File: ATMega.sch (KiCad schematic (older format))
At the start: 28 parts, among them J14 Conn_02x03_Odd_Even, SW1 SW_Push, U2 ATmega2560-16AU, Y1 16MHz

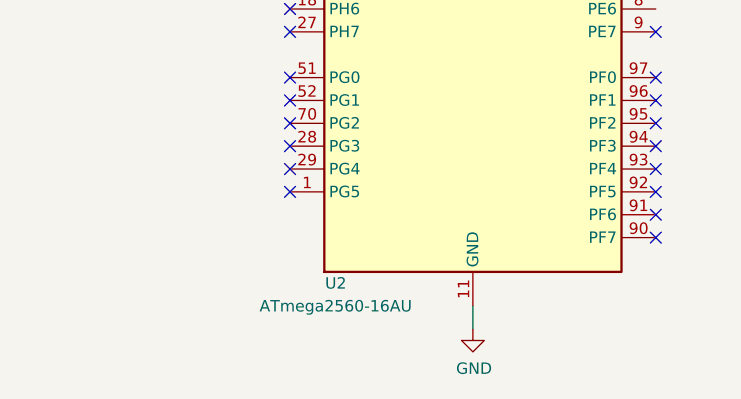
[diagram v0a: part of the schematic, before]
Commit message: LMZM23600 from official kicad lib
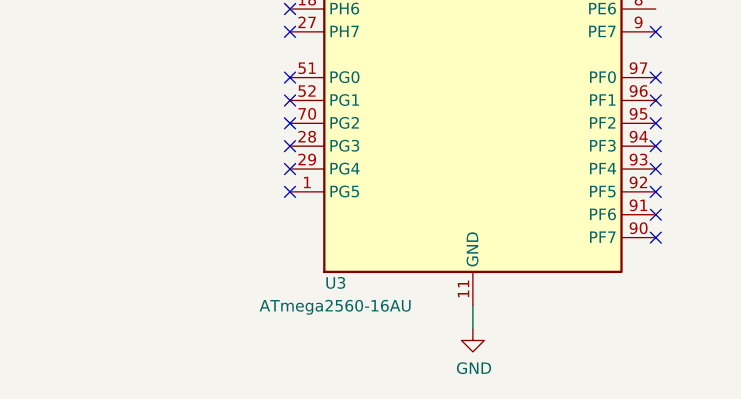
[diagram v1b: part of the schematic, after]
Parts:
- renumbered U2 to U3
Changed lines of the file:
@@
 	4300 5350 4250 5350
 $Comp
-L MCU_Microchip_ATmega:ATmega2560-16AU U2
+L MCU_Microchip_ATmega:ATmega2560-16AU U3
 U 1 1 5C280BF8
 P 3450 3950
-F 0 "U2" H 2850 1150 50  0000 C CNN
+F 0 "U3" H 2850 1150 50  0000 C CNN
 F 1 "ATmega2560-16AU" H 2850 1050 50  0000 C CNN
 F 2 "Package_QFP:TQFP-100_14x14mm_P0.5mm" H 3450 3950 50  0001 C CIN

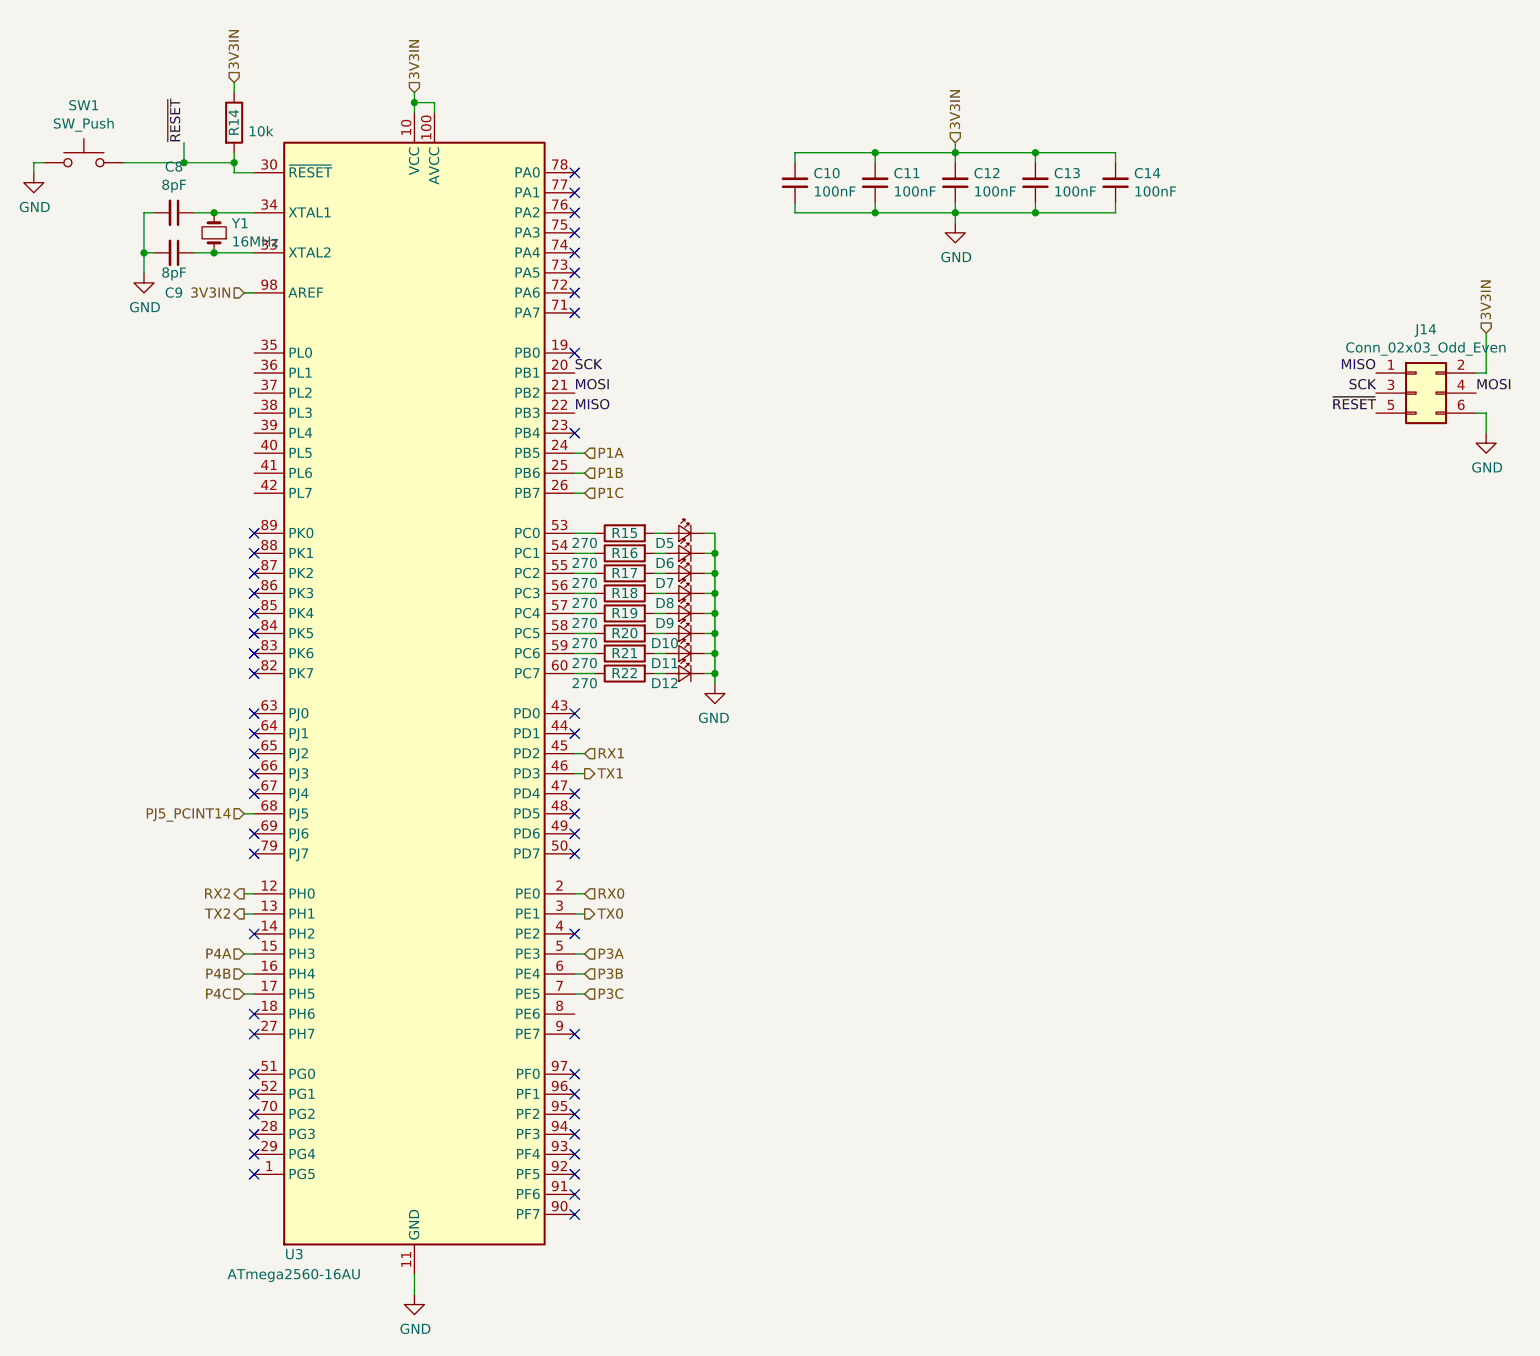
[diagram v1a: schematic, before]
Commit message: use submodule for FT230
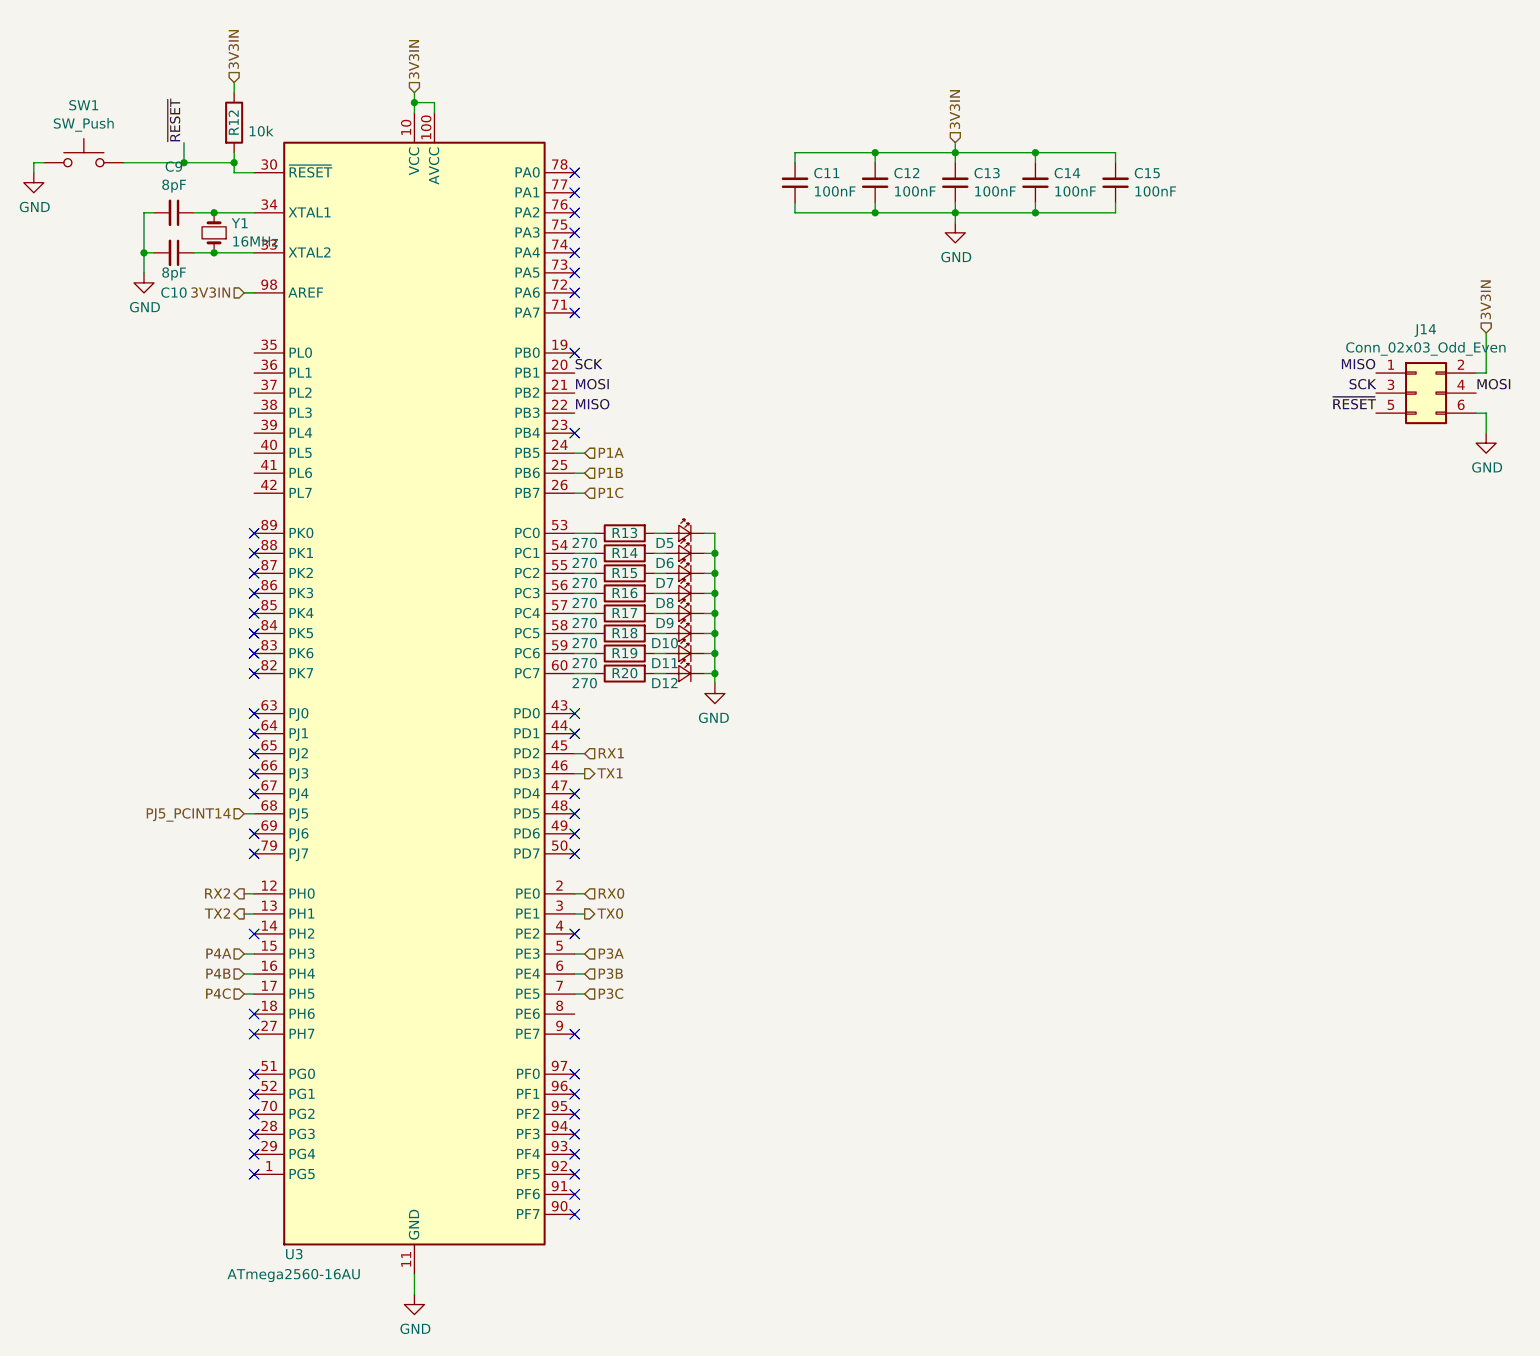
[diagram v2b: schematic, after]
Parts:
- renumbered C9 to C10, C10 to C11, C11 to C12, C12 to C13, C13 to C14, C14 to C15, C8 to C9, R14 to R12, R15 to R13, R16 to R14, R17 to R15, R18 to R16, R19 to R17, R20 to R18, R21 to R19, R22 to R20
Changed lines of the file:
@@
 	2450 1750 2650 1750
 $Comp
-L Device:C_Small C8
+L Device:C_Small C9
 U 1 1 5C2814DA
 P 2250 1550
-F 0 "C8" V 2021 1550 50  0000 C CNN
+F 0 "C9" V 2021 1550 50  0000 C CNN
 F 1 "8pF" V 2112 1550 50  0000 C CNN
 F 2 "Capacitor_SMD:C_0603_1608Metric" H 2250 1550 50  0001 C CNN
@@
 $EndComp
 $Comp
-L Device:C_Small C9
+L Device:C_Small C10
 U 1 1 5C281519
 P 2250 1750
-F 0 "C9" V 2450 1750 50  0000 C CNN
+F 0 "C10" V 2450 1750 50  0000 C CNN
 F 1 "8pF" V 2350 1750 50  0000 C CNN
 F 2 "Capacitor_SMD:C_0603_1608Metric" H 2250 1750 50  0001 C CNN
@@
 Connection ~ 2100 1750
 $Comp
-L Device:R R15
+L Device:R R13
 U 1 1 5C281CF1
 P 4500 3150
-F 0 "R15" V 4500 3150 50  0000 C CNN
+F 0 "R13" V 4500 3150 50  0000 C CNN
 F 1 "270" V 4550 3350 50  0000 C CNN
 F 2 "Resistor_SMD:R_0603_1608Metric" V 4430 3150 50  0001 C CNN
@@
 $EndComp
 $Comp
-L Device:R R16
+L Device:R R14
 U 1 1 5C281E2C
 P 4500 3250
-F 0 "R16" V 4500 3250 50  0000 C CNN
+F 0 "R14" V 4500 3250 50  0000 C CNN
 F 1 "270" V 4550 3450 50  0000 C CNN
 F 2 "Resistor_SMD:R_0603_1608Metric" V 4430 3250 50  0001 C CNN
@@
 $EndComp
 $Comp
-L Device:R R17
+L Device:R R15
 U 1 1 5C281E58
 P 4500 3350
-F 0 "R17" V 4500 3350 50  0000 C CNN
+F 0 "R15" V 4500 3350 50  0000 C CNN
 F 1 "270" V 4550 3550 50  0000 C CNN
 F 2 "Resistor_SMD:R_0603_1608Metric" V 4430 3350 50  0001 C CNN
@@
 $EndComp
 $Comp
-L Device:R R18
+L Device:R R16
 U 1 1 5C281E76
 P 4500 3450
-F 0 "R18" V 4500 3450 50  0000 C CNN
+F 0 "R16" V 4500 3450 50  0000 C CNN
 F 1 "270" V 4550 3650 50  0000 C CNN
 F 2 "Resistor_SMD:R_0603_1608Metric" V 4430 3450 50  0001 C CNN
@@
 	4950 3450 4950 3350
 $Comp
-L Device:R R14
+L Device:R R12
 U 1 1 5C28BE77
 P 2550 1100
-F 0 "R14" V 2550 1100 50  0000 C CNN
+F 0 "R12" V 2550 1100 50  0000 C CNN
 F 1 "10k" H 2620 1055 50  0000 L CNN
 F 2 "Resistor_SMD:R_0603_1608Metric" V 2480 1100 50  0001 C CNN
@@
 	2600 1950 2650 1950
 $Comp
-L Device:C_Small C10
+L Device:C_Small C11
 U 1 1 5C28F5ED
 P 5350 1400
-F 0 "C10" H 5258 1354 50  0000 R CNN
+F 0 "C11" H 5258 1354 50  0000 R CNN
 F 1 "100nF" H 5258 1445 50  0000 R CNN
 F 2 "Capacitor_SMD:C_0603_1608Metric" H 5350 1400 50  0001 C CNN
@@
 $EndComp
 $Comp
-L Device:C_Small C11
+L Device:C_Small C12
 U 1 1 5C28FBD2
 P 5750 1400
-F 0 "C11" H 5658 1354 50  0000 R CNN
+F 0 "C12" H 5658 1354 50  0000 R CNN
 F 1 "100nF" H 5658 1445 50  0000 R CNN
 F 2 "Capacitor_SMD:C_0603_1608Metric" H 5750 1400 50  0001 C CNN
@@
 $EndComp
 $Comp
-L Device:C_Small C12
+L Device:C_Small C13
 U 1 1 5C28FC1A
 P 6150 1400
-F 0 "C12" H 6058 1354 50  0000 R CNN
+F 0 "C13" H 6058 1354 50  0000 R CNN
 F 1 "100nF" H 6058 1445 50  0000 R CNN
 F 2 "Capacitor_SMD:C_0603_1608Metric" H 6150 1400 50  0001 C CNN
@@
 $EndComp
 $Comp
-L Device:C_Small C13
+L Device:C_Small C14
 U 1 1 5C28FC66
 P 6550 1400
-F 0 "C13" H 6458 1354 50  0000 R CNN
+F 0 "C14" H 6458 1354 50  0000 R CNN
 F 1 "100nF" H 6458 1445 50  0000 R CNN
 F 2 "Capacitor_SMD:C_0603_1608Metric" H 6550 1400 50  0001 C CNN
@@
 $EndComp
 $Comp
-L Device:C_Small C14
+L Device:C_Small C15
 U 1 1 5C28FCBA
 P 6950 1400
-F 0 "C14" H 6858 1354 50  0000 R CNN
+F 0 "C15" H 6858 1354 50  0000 R CNN
 F 1 "100nF" H 6858 1445 50  0000 R CNN
 F 2 "Capacitor_SMD:C_0603_1608Metric" H 6950 1400 50  0001 C CNN
@@
 NoConn ~ 4250 6550
 $Comp
-L Device:R R19
+L Device:R R17
 U 1 1 5C923641
 P 4500 3550
-F 0 "R19" V 4500 3550 50  0000 C CNN
+F 0 "R17" V 4500 3550 50  0000 C CNN
 F 1 "270" V 4550 3750 50  0000 C CNN
 F 2 "Resistor_SMD:R_0603_1608Metric" V 4430 3550 50  0001 C CNN
@@
 $EndComp
 $Comp
-L Device:R R20
+L Device:R R18
 U 1 1 5C923A5C
 P 4500 3650
-F 0 "R20" V 4500 3650 50  0000 C CNN
+F 0 "R18" V 4500 3650 50  0000 C CNN
 F 1 "270" V 4550 3850 50  0000 C CNN
 F 2 "Resistor_SMD:R_0603_1608Metric" V 4430 3650 50  0001 C CNN
@@
 $EndComp
 $Comp
-L Device:R R21
+L Device:R R19
 U 1 1 5C923B7C
 P 4500 3750
-F 0 "R21" V 4500 3750 50  0000 C CNN
+F 0 "R19" V 4500 3750 50  0000 C CNN
 F 1 "270" V 4550 3950 50  0000 C CNN
 F 2 "Resistor_SMD:R_0603_1608Metric" V 4430 3750 50  0001 C CNN
@@
 $EndComp
 $Comp
-L Device:R R22
+L Device:R R20
 U 1 1 5C923CFF
 P 4500 3850
-F 0 "R22" V 4500 3850 50  0000 C CNN
+F 0 "R20" V 4500 3850 50  0000 C CNN
 F 1 "270" V 4550 4050 50  0000 C CNN
 F 2 "Resistor_SMD:R_0603_1608Metric" V 4430 3850 50  0001 C CNN

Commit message: pullups, jumpers
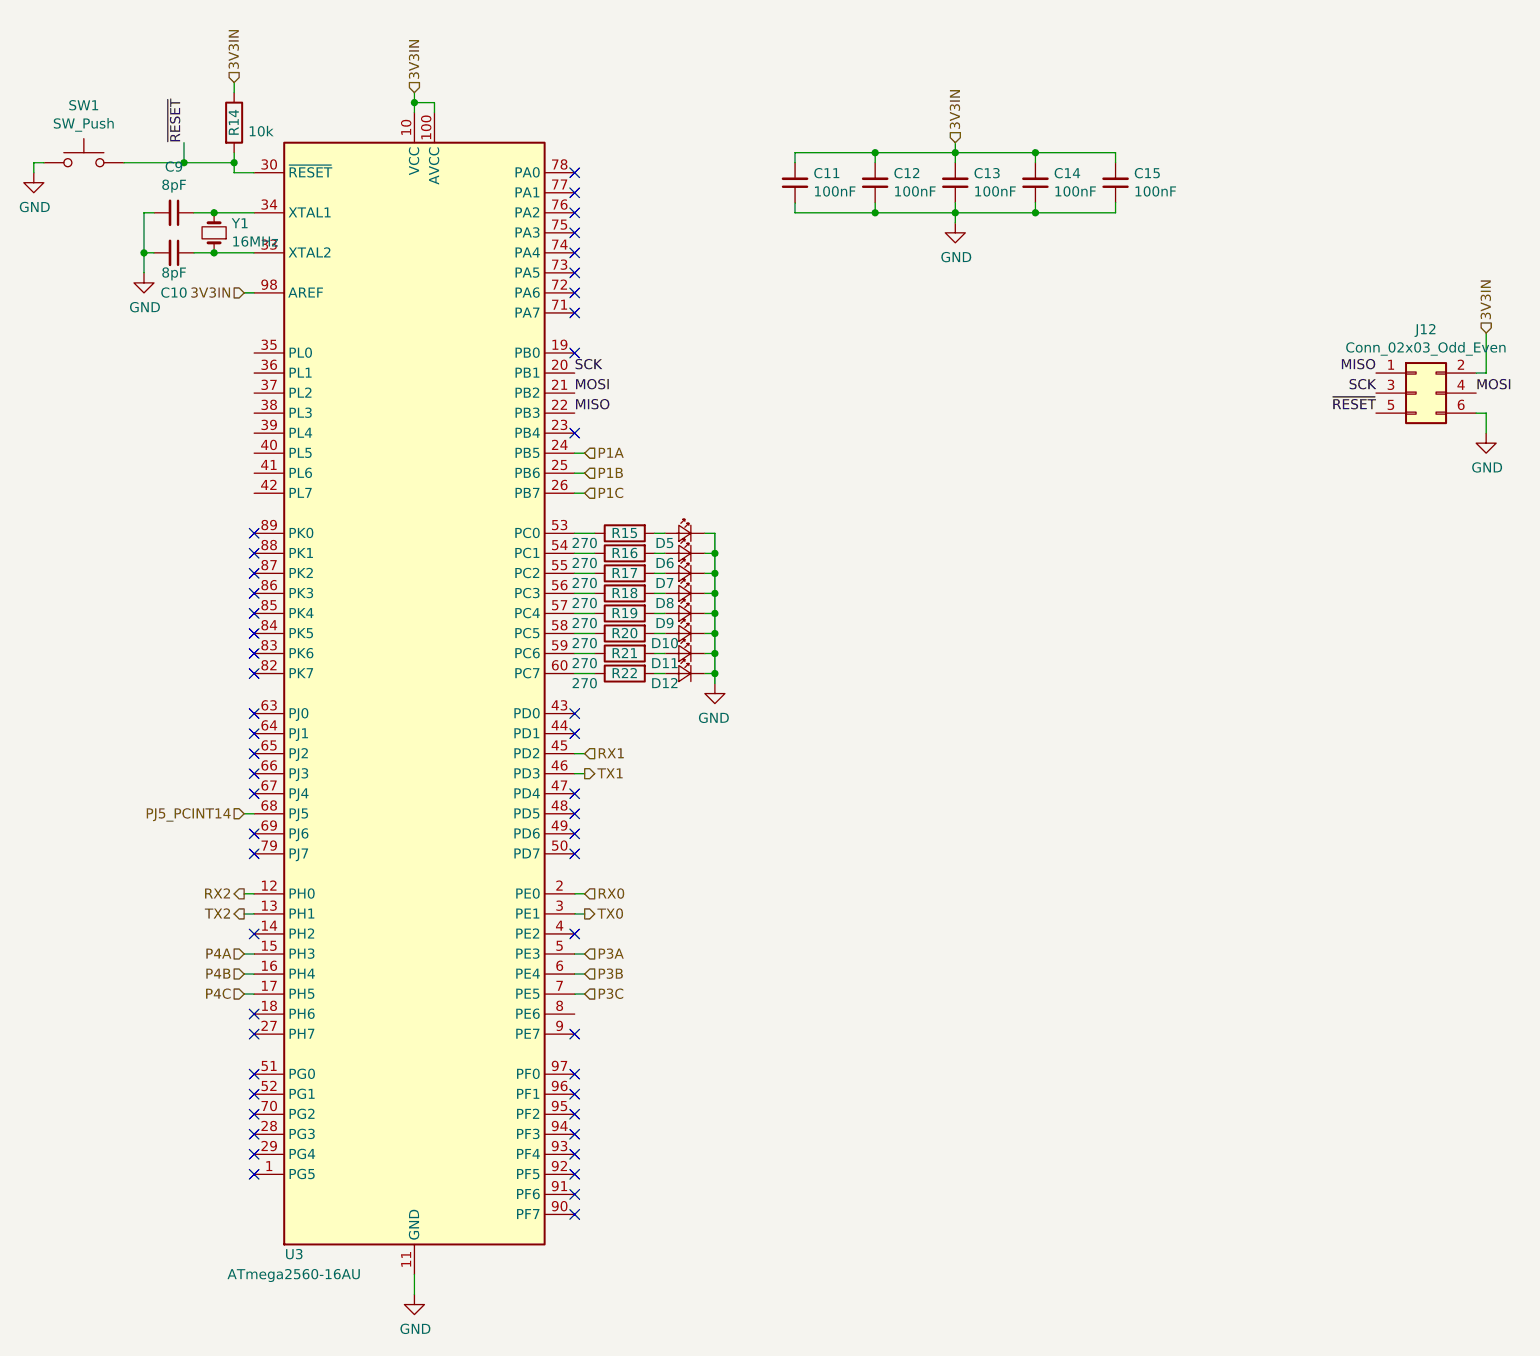
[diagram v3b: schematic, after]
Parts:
- renumbered J14 to J12, R12 to R14, R13 to R15, R14 to R16, R15 to R17, R16 to R18, R17 to R19, R18 to R20, R19 to R21, R20 to R22
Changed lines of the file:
@@
 Connection ~ 2100 1750
 $Comp
-L Device:R R13
+L Device:R R15
 U 1 1 5C281CF1
 P 4500 3150
-F 0 "R13" V 4500 3150 50  0000 C CNN
+F 0 "R15" V 4500 3150 50  0000 C CNN
 F 1 "270" V 4550 3350 50  0000 C CNN
 F 2 "Resistor_SMD:R_0603_1608Metric" V 4430 3150 50  0001 C CNN
@@
 $EndComp
 $Comp
-L Device:R R14
+L Device:R R16
 U 1 1 5C281E2C
 P 4500 3250
-F 0 "R14" V 4500 3250 50  0000 C CNN
+F 0 "R16" V 4500 3250 50  0000 C CNN
 F 1 "270" V 4550 3450 50  0000 C CNN
 F 2 "Resistor_SMD:R_0603_1608Metric" V 4430 3250 50  0001 C CNN
@@
 $EndComp
 $Comp
-L Device:R R15
+L Device:R R17
 U 1 1 5C281E58
 P 4500 3350
-F 0 "R15" V 4500 3350 50  0000 C CNN
+F 0 "R17" V 4500 3350 50  0000 C CNN
 F 1 "270" V 4550 3550 50  0000 C CNN
 F 2 "Resistor_SMD:R_0603_1608Metric" V 4430 3350 50  0001 C CNN
@@
 $EndComp
 $Comp
-L Device:R R16
+L Device:R R18
 U 1 1 5C281E76
 P 4500 3450
-F 0 "R16" V 4500 3450 50  0000 C CNN
+F 0 "R18" V 4500 3450 50  0000 C CNN
 F 1 "270" V 4550 3650 50  0000 C CNN
 F 2 "Resistor_SMD:R_0603_1608Metric" V 4430 3450 50  0001 C CNN
@@
 	4950 3450 4950 3350
 $Comp
-L Device:R R12
+L Device:R R14
 U 1 1 5C28BE77
 P 2550 1100
-F 0 "R12" V 2550 1100 50  0000 C CNN
+F 0 "R14" V 2550 1100 50  0000 C CNN
 F 1 "10k" H 2620 1055 50  0000 L CNN
 F 2 "Resistor_SMD:R_0603_1608Metric" V 2480 1100 50  0001 C CNN
@@
 	6150 1250 6150 1200
 $Comp
-L Connector_Generic:Conn_02x03_Odd_Even J14
+L Connector_Generic:Conn_02x03_Odd_Even J12
 U 1 1 5C29DEFC
 P 8450 2450
-F 0 "J14" H 8500 2767 50  0000 C CNN
+F 0 "J12" H 8500 2767 50  0000 C CNN
 F 1 "Conn_02x03_Odd_Even" H 8500 2676 50  0000 C CNN
 F 2 "Connector_PinHeader_2.54mm:PinHeader_2x03_P2.54mm_Vertical" H 8450 2450 50  0001 C CNN
@@
 NoConn ~ 4250 6550
 $Comp
-L Device:R R17
+L Device:R R19
 U 1 1 5C923641
 P 4500 3550
-F 0 "R17" V 4500 3550 50  0000 C CNN
+F 0 "R19" V 4500 3550 50  0000 C CNN
 F 1 "270" V 4550 3750 50  0000 C CNN
 F 2 "Resistor_SMD:R_0603_1608Metric" V 4430 3550 50  0001 C CNN
@@
 $EndComp
 $Comp
-L Device:R R18
+L Device:R R20
 U 1 1 5C923A5C
 P 4500 3650
-F 0 "R18" V 4500 3650 50  0000 C CNN
+F 0 "R20" V 4500 3650 50  0000 C CNN
 F 1 "270" V 4550 3850 50  0000 C CNN
 F 2 "Resistor_SMD:R_0603_1608Metric" V 4430 3650 50  0001 C CNN
@@
 $EndComp
 $Comp
-L Device:R R19
+L Device:R R21
 U 1 1 5C923B7C
 P 4500 3750
-F 0 "R19" V 4500 3750 50  0000 C CNN
+F 0 "R21" V 4500 3750 50  0000 C CNN
 F 1 "270" V 4550 3950 50  0000 C CNN
 F 2 "Resistor_SMD:R_0603_1608Metric" V 4430 3750 50  0001 C CNN
@@
 $EndComp
 $Comp
-L Device:R R20
+L Device:R R22
 U 1 1 5C923CFF
 P 4500 3850
-F 0 "R20" V 4500 3850 50  0000 C CNN
+F 0 "R22" V 4500 3850 50  0000 C CNN
 F 1 "270" V 4550 4050 50  0000 C CNN
 F 2 "Resistor_SMD:R_0603_1608Metric" V 4430 3850 50  0001 C CNN
